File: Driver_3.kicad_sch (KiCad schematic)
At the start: 34 parts

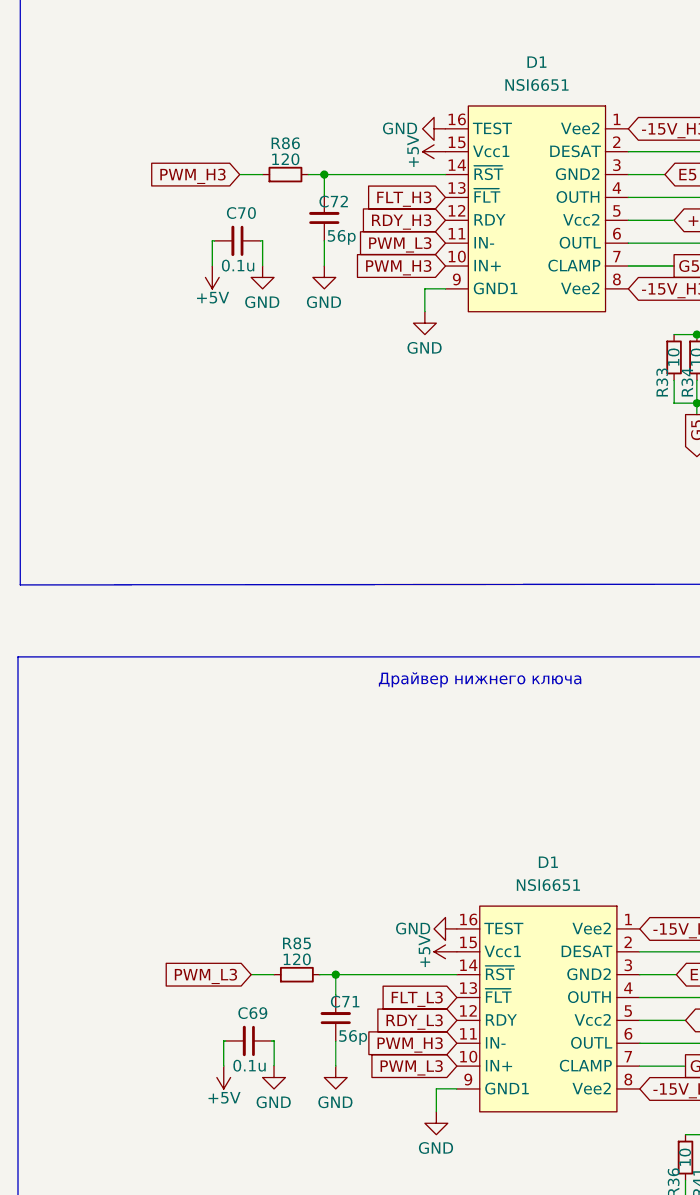
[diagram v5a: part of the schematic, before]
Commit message: Развел стойку фазы А
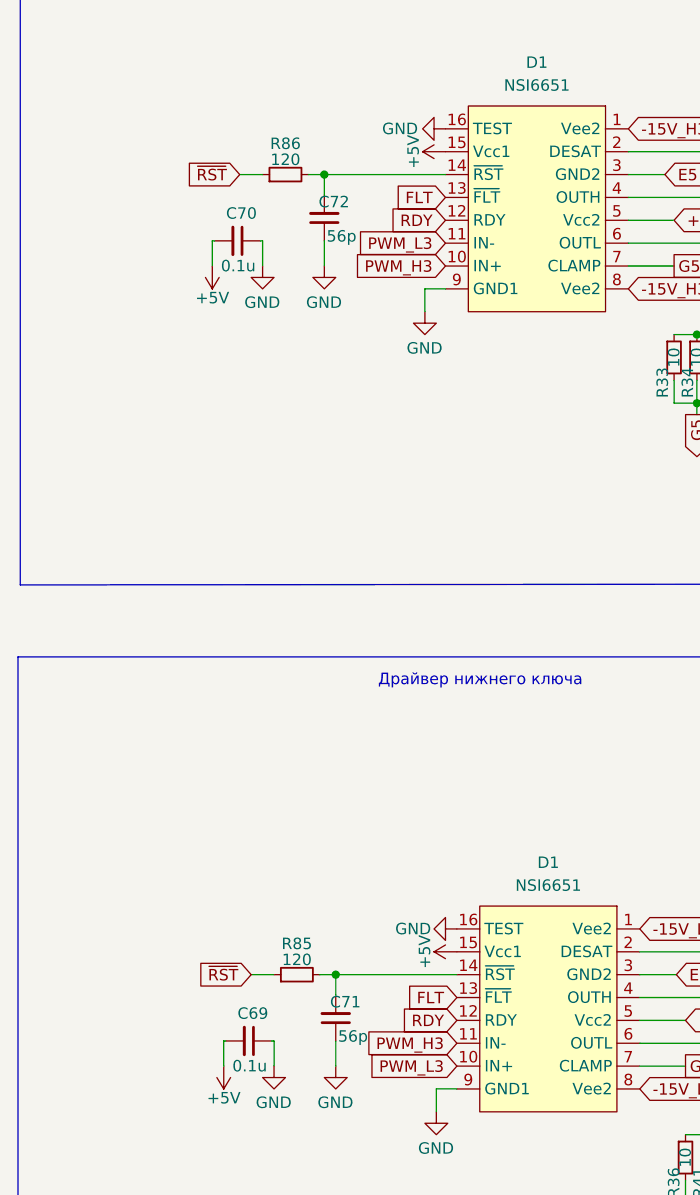
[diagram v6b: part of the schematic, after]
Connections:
- net FLT_L3 is gone; now on net FLT: D1.13 (~{FLT})
- net RDY_L3 is gone; now on net RDY: D1.12 (RDY)
- net PWM_H3: no longer R86.1
- net PWM_L3: no longer R85.1
- net FLT_H3 renamed FLT
- net RDY_H3 renamed RDY
- new net ~{RST}: R85.1, R86.1

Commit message: Развел вторую стойку
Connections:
- net FLT renamed FLT_C
- net RDY renamed RDY_C
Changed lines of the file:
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@@
 		)
 	)
-	(global_label "RDY"
+	(global_label "RDY_C"
 		(shape input)
 		(at 78.74 59.69 180)
@@
 		)
 		(property "Intersheetrefs" "${INTERSHEET_REFS}"
-			(at 72.7984 59.69 0)
+			(at 69.8886 59.69 0)
 			(effects
 				(font
@@
 		)
 	)
-	(global_label "FLT"
+	(global_label "FLT_C"
 		(shape input)
 		(at 78.74 57.15 180)
@@
 		)
 		(property "Intersheetrefs" "${INTERSHEET_REFS}"
-			(at 73.1806 57.15 0)
+			(at 70.4329 57.15 0)
 			(effects
 				(font
@@
 		)
 	)
-	(global_label "RDY"
+	(global_label "RDY_C"
 		(shape input)
 		(at 80.01 148.59 180)
@@
 		)
 		(property "Intersheetrefs" "${INTERSHEET_REFS}"
-			(at 74.0684 148.59 0)
+			(at 71.1586 148.59 0)
 			(effects
 				(font
@@
 		)
 	)
-	(global_label "FLT"
+	(global_label "FLT_C"
 		(shape input)
 		(at 80.01 146.05 180)
@@
 		)
 		(property "Intersheetrefs" "${INTERSHEET_REFS}"
-			(at 74.4506 146.05 0)
-			(effects
-				(font
+			(at 71.7029 146.05 0)
+			(effects
+				(font
